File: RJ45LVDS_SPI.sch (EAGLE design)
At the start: 45 parts, among them J1 RJHSE-3381, U1 SN65MLVD206, U2 SN65MLVD206, U3 SN65MLVD206, U4 SN65MLVD206, U5 SN74LVC1T45DBVR, U6 SN74LVC1T45DBVR, U7 SN74LVC1T45DBVR, U8 SN74LVC1T45DBVR, U9 MIC39100-3.3WS

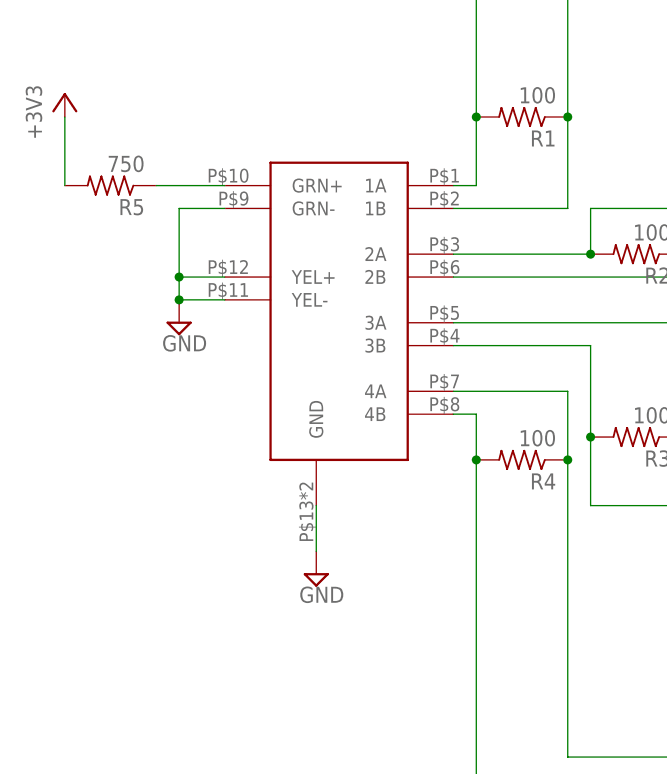
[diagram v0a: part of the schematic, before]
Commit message: Changed RJ45 footprint
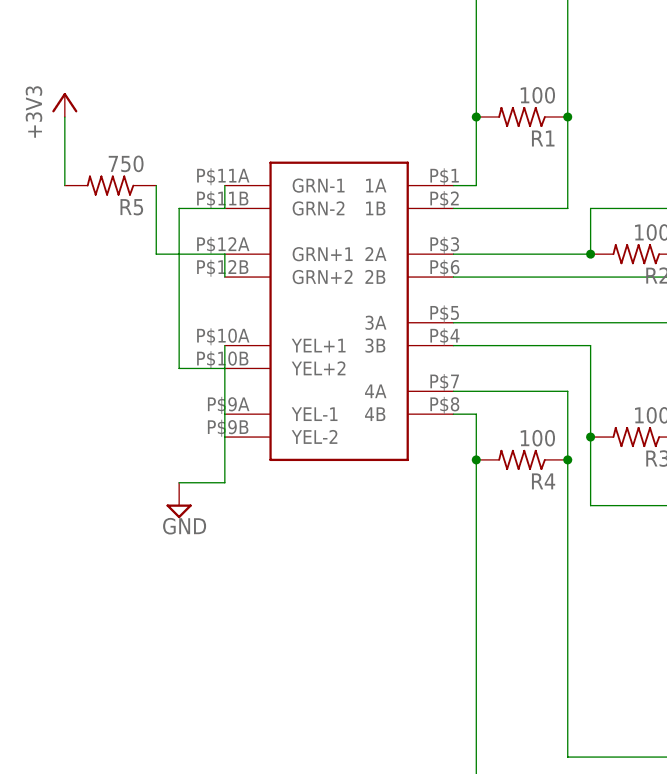
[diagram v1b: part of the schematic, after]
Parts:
- removed J1: RJHSE-3381, artiq-ttl:RJHSE-3381
- added J2: MRJ, artiq-ttl:MRJ
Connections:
- net GND: now also J2.GRN-1, J2.GRN-2, J2.YEL+1, J2.YEL+2, J2.YEL-1, J2.YEL-2; no longer J1.GND, J1.GRN-, J1.YEL+, J1.YEL-
- net IN1_N: now also J2.1B; no longer J1.1B
- net IN1_P: now also J2.1A; no longer J1.1A
- net IN2_N: now also J2.2B; no longer J1.2B
- net IN2_P: now also J2.2A; no longer J1.2A
- net IN3_N: now also J2.3B; no longer J1.3B
- net IN3_P: now also J2.3A; no longer J1.3A
- net IN4_N: now also J2.4B; no longer J1.4B
- net IN4_P: now also J2.4A; no longer J1.4A
- net N$19: now also J2.GRN+1, J2.GRN+2; no longer J1.GRN+

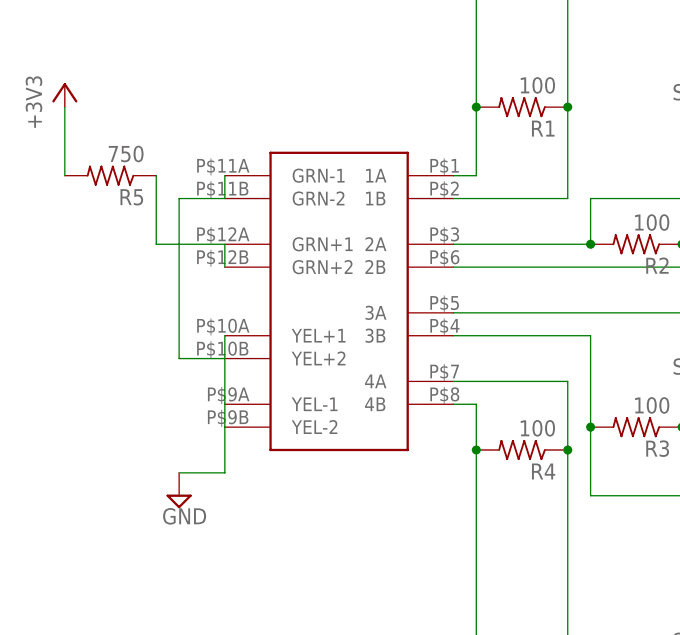
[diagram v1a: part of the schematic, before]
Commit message: Fixed RJ45 footprint issue
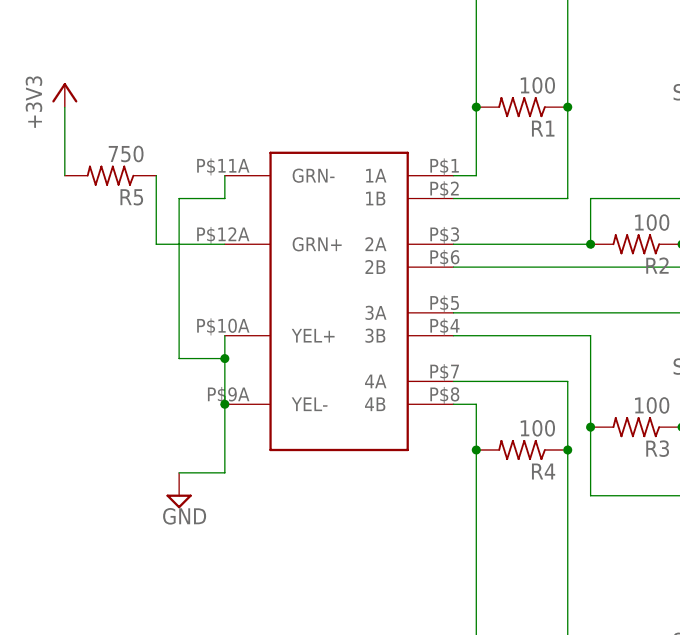
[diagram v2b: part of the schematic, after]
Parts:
- removed J2: MRJ, artiq-ttl:MRJ
- added J1: MRJ, RJ45LVDS_SPI:MRJ
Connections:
- net GND: now also J1.GRN-, J1.YEL+, J1.YEL-; no longer J2.GRN-1, J2.GRN-2, J2.YEL+1, J2.YEL+2, J2.YEL-1, J2.YEL-2
- net IN1_N: now also J1.1B; no longer J2.1B
- net IN1_P: now also J1.1A; no longer J2.1A
- net IN2_N: now also J1.2B; no longer J2.2B
- net IN2_P: now also J1.2A; no longer J2.2A
- net IN3_N: now also J1.3B; no longer J2.3B
- net IN3_P: now also J1.3A; no longer J2.3A
- net IN4_N: now also J1.4B; no longer J2.4B
- net IN4_P: now also J1.4A; no longer J2.4A
- net N$19: now also J1.GRN+; no longer J2.GRN+1, J2.GRN+2
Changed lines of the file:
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@@
 <part name="+3V8" library="supply1" deviceset="+3V3" device=""/>
 <part name="+3V9" library="supply1" deviceset="+3V3" device=""/>
-<part name="J2" library="artiq-ttl" deviceset="MRJ" device=""/>
+<part name="J1" library="RJ45LVDS_SPI" deviceset="MRJ" device=""/>
 </parts>
 <sheets>
@@
 <instance part="+3V8" gate="G$1" x="40.64" y="160.02"/>
 <instance part="+3V9" gate="G$1" x="114.3" y="127"/>
-<instance part="J2" gate="G$1" x="-78.74" y="58.42"/>
+<instance part="J1" gate="G$1" x="-78.74" y="58.42"/>
 </instances>
 <busses>
@@
 <pinref part="R4" gate="G$1" pin="1"/>
 <junction x="-55.88" y="43.18"/>
-<pinref part="J2" gate="G$1" pin="4A"/>
+<pinref part="J1" gate="G$1" pin="4A"/>
 </segment>
 </net>
@@
 <wire x1="-43.18" y1="45.72" x2="-43.18" y2="40.64" width="0.1524" layer="91"/>
 <junction x="-43.18" y="45.72"/>
-<pinref part="J2" gate="G$1" pin="3A"/>
+<pinref part="J1" gate="G$1" pin="3A"/>
 </segment>
 </net>
@@
 <pinref part="R2" gate="G$1" pin="2"/>
 <junction x="-53.34" y="66.04"/>
-<pinref part="J2" gate="G$1" pin="2A"/>
+<pinref part="J1" gate="G$1" pin="2A"/>
 </segment>
 </net>
@@
 <wire x1="-66.04" y1="81.28" x2="-66.04" y2="73.66" width="0.1524" layer="91"/>
 <junction x="-66.04" y="81.28"/>
-<pinref part="J2" gate="G$1" pin="1A"/>
+<pinref part="J1" gate="G$1" pin="1A"/>
 </segment>
 </net>
@@
 <junction x="-55.88" y="81.28"/>
 <wire x1="-68.58" y1="71.12" x2="-55.88" y2="71.12" width="0.1524" layer="91"/>
-<pinref part="J2" gate="G$1" pin="1B"/>
+<pinref part="J1" gate="G$1" pin="1B"/>
 </segment>
 </net>
@@
 <pinref part="R2" gate="G$1" pin="1"/>
 <junction x="-43.18" y="66.04"/>
-<pinref part="J2" gate="G$1" pin="2B"/>
+<pinref part="J1" gate="G$1" pin="2B"/>
 </segment>
 </net>
@@
 <pinref part="R3" gate="G$1" pin="2"/>
 <junction x="-53.34" y="45.72"/>
-<pinref part="J2" gate="G$1" pin="3B"/>
+<pinref part="J1" gate="G$1" pin="3B"/>
 </segment>
 </net>
@@
 <pinref part="R4" gate="G$1" pin="2"/>
 <junction x="-66.04" y="43.18"/>
-<pinref part="J2" gate="G$1" pin="4B"/>
+<pinref part="J1" gate="G$1" pin="4B"/>
 </segment>
 </net>
@@
 </segment>
 <segment>
-<pinref part="J2" gate="G$1" pin="GRN-1"/>
-<pinref part="J2" gate="G$1" pin="GRN-2"/>
+<pinref part="SUPPLY28" gate="GND" pin="GND"/>
+<wire x1="-93.98" y1="40.64" x2="-99.06" y2="40.64" width="0.1524" layer="91"/>
+<wire x1="-93.98" y1="48.26" x2="-93.98" y2="40.64" width="0.1524" layer="91"/>
+<pinref part="J1" gate="G$1" pin="YEL-"/>
+<junction x="-93.98" y="48.26"/>
+<wire x1="-93.98" y1="55.88" x2="-93.98" y2="53.34" width="0.1524" layer="91"/>
+<pinref part="J1" gate="G$1" pin="YEL+"/>
+<wire x1="-93.98" y1="53.34" x2="-93.98" y2="48.26" width="0.1524" layer="91"/>
 <wire x1="-93.98" y1="71.12" x2="-93.98" y2="73.66" width="0.1524" layer="91"/>
 <wire x1="-93.98" y1="71.12" x2="-99.06" y2="71.12" width="0.1524" layer="91"/>
 <wire x1="-99.06" y1="71.12" x2="-99.06" y2="53.34" width="0.1524" layer="91"/>
-<pinref part="J2" gate="G$1" pin="YEL-2"/>
-<pinref part="J2" gate="G$1" pin="YEL-1"/>
-<wire x1="-93.98" y1="45.72" x2="-93.98" y2="48.26" width="0.1524" layer="91"/>
-<pinref part="J2" gate="G$1" pin="YEL+2"/>
-<wire x1="-93.98" y1="48.26" x2="-93.98" y2="53.34" width="0.1524" layer="91"/>
-<pinref part="J2" gate="G$1" pin="YEL+1"/>
-<wire x1="-93.98" y1="53.34" x2="-93.98" y2="55.88" width="0.1524" layer="91"/>
+<pinref part="J1" gate="G$1" pin="GRN-"/>
 <wire x1="-99.06" y1="53.34" x2="-93.98" y2="53.34" width="0.1524" layer="91"/>
-<wire x1="-93.98" y1="45.72" x2="-93.98" y2="40.64" width="0.1524" layer="91"/>
-<pinref part="SUPPLY28" gate="GND" pin="GND"/>
-<wire x1="-93.98" y1="40.64" x2="-99.06" y2="40.64" width="0.1524" layer="91"/>
+<junction x="-93.98" y="53.34"/>
 </segment>
 </net>
@@
 <net name="N$19" class="0">
 <segment>
-<pinref part="J2" gate="G$1" pin="GRN+2"/>
-<pinref part="J2" gate="G$1" pin="GRN+1"/>
-<wire x1="-93.98" y1="63.5" x2="-93.98" y2="66.04" width="0.1524" layer="91"/>
 <wire x1="-93.98" y1="66.04" x2="-101.6" y2="66.04" width="0.1524" layer="91"/>
 <pinref part="R5" gate="G$1" pin="1"/>
 <wire x1="-101.6" y1="66.04" x2="-101.6" y2="73.66" width="0.1524" layer="91"/>
-</segment>
-</net>
+<pinref part="J1" gate="G$1" pin="GRN+"/>
+</segment>
+</net>

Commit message: v0.4 changes
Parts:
- added C17: .1u, rcl-dhs:C-USC0603
- added JP3: (no value), pinhead:PINHD-1X2
- added U10: 74AHC1GU04DCK, 74xx-little-us:74AHC1GU04DCK
- JP1: device pinhead:PINHD-2X5 -> pinhead:PINHD-2X6
- SJ1, SJ2, SJ3, SJ4, SJ5, SJ6, SJ7, SJ8: device jumper:SJ2W -> RJ45LVDS_SPI:SJ2W
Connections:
- new net A: JP3.1, U10G$1.I
- new net NOT_A: JP3.2, U10G$1.O
- net +3V3: now also JP1.1, JP1.2
- net GND: now also C17.2, JP1.3, JP1.4, U10G$2.GND; no longer JP1.1, JP1.2
- net N$13: now also JP1.5, JP1.6; no longer JP1.3, JP1.4
- net N$14: now also JP1.7, JP1.8; no longer JP1.5, JP1.6
- net N$15: now also JP1.10, JP1.9; no longer JP1.7, JP1.8
- net N$8: now also JP1.11, JP1.12; no longer JP1.10, JP1.9
- net VCCIO: now also C17.1, U10G$2.VCC
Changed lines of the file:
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@@
 <layer number="91" name="Nets" color="2" fill="1" visible="yes" active="yes"/>
 <layer number="92" name="Busses" color="1" fill="1" visible="yes" active="yes"/>
-<layer number="93" name="Pins" color="2" fill="1" visible="no" active="yes"/>
+<layer number="93" name="Pins" color="2" fill="1" visible="yes" active="yes"/>
 <layer number="94" name="Symbols" color="4" fill="1" visible="yes" active="yes"/>
 <layer number="95" name="Names" color="7" fill="1" visible="yes" active="yes"/>
@@
 <part name="C8" library="rcl-dhs" deviceset="C-US" device="C0603" value=".1u"/>
 <part name="SUPPLY28" library="supply2" deviceset="GND" device=""/>
-<part name="SJ1" library="jumper" deviceset="SJ2W" device=""/>
-<part name="SJ2" library="jumper" deviceset="SJ2W" device=""/>
-<part name="SJ3" library="jumper" deviceset="SJ2W" device=""/>
-<part name="SJ4" library="jumper" deviceset="SJ2W" device=""/>
+<part name="SJ1" library="RJ45LVDS_SPI" deviceset="SJ2W" device=""/>
+<part name="SJ2" library="RJ45LVDS_SPI" deviceset="SJ2W" device=""/>
+<part name="SJ3" library="RJ45LVDS_SPI" deviceset="SJ2W" device=""/>
+<part name="SJ4" library="RJ45LVDS_SPI" deviceset="SJ2W" device=""/>
 <part name="U5" library="SN74LVC1T45DBVR" deviceset="SN74LVC1T45DBVR" device=""/>
 <part name="U6" library="SN74LVC1T45DBVR" deviceset="SN74LVC1T45DBVR" device=""/>
@@
 <part name="U8" library="SN74LVC1T45DBVR" deviceset="SN74LVC1T45DBVR" device=""/>
 <part name="+3V6" library="supply1" deviceset="+3V3" device=""/>
-<part name="SJ5" library="jumper" deviceset="SJ2W" device=""/>
-<part name="SJ6" library="jumper" deviceset="SJ2W" device=""/>
-<part name="SJ7" library="jumper" deviceset="SJ2W" device=""/>
-<part name="SJ8" library="jumper" deviceset="SJ2W" device=""/>
+<part name="SJ5" library="RJ45LVDS_SPI" deviceset="SJ2W" device=""/>
+<part name="SJ6" library="RJ45LVDS_SPI" deviceset="SJ2W" device=""/>
+<part name="SJ7" library="RJ45LVDS_SPI" deviceset="SJ2W" device=""/>
+<part name="SJ8" library="RJ45LVDS_SPI" deviceset="SJ2W" device=""/>
 <part name="SUPPLY6" library="supply2" deviceset="GND" device=""/>
 <part name="SJ9" library="rcl-dhs" deviceset="JUMPER" device=""/>
@@
 <part name="C6" library="rcl-dhs" deviceset="C-US" device="C0603" value=".1u"/>
 <part name="C7" library="rcl-dhs" deviceset="C-US" device="C0603" value=".1u"/>
-<part name="JP1" library="pinhead" deviceset="PINHD-2X5" device=""/>
 <part name="JP2" library="pinhead" deviceset="PINHD-1X4" device=""/>
 <part name="C12" library="rcl-dhs" deviceset="C-US" device="C0603" value=".1u"/>
@@
 <part name="+3V9" library="supply1" deviceset="+3V3" device=""/>
 <part name="J1" library="RJ45LVDS_SPI" deviceset="MRJ" device=""/>
+<part name="JP1" library="pinhead" deviceset="PINHD-2X6" device=""/>
+<part name="+3V10" library="supply1" deviceset="+3V3" device=""/>
+<part name="U10" library="74xx-little-us" deviceset="74*1GU04" device="DCK" technology="AHC"/>
+<part name="JP3" library="pinhead" deviceset="PINHD-1X2" device=""/>
+<part name="VCC4" library="supply1" deviceset="VCCIO" device=""/>
+<part name="SUPPLY1" library="supply2" deviceset="GND" device=""/>
+<part name="C17" library="rcl-dhs" deviceset="C-US" device="C0603" value=".1u"/>
 </parts>
 <sheets>
@@
 <instance part="C6" gate="G$1" x="55.88" y="187.96"/>
 <instance part="C7" gate="G$1" x="66.04" y="187.96"/>
-<instance part="JP1" gate="A" x="160.02" y="53.34"/>
 <instance part="JP2" gate="A" x="180.34" y="106.68"/>
 <instance part="C12" gate="G$1" x="111.76" y="157.48" rot="R180"/>
@@
 <instance part="+3V9" gate="G$1" x="114.3" y="127"/>
 <instance part="J1" gate="G$1" x="-78.74" y="58.42"/>
+<instance part="JP1" gate="A" x="160.02" y="55.88"/>
+<instance part="+3V10" gate="G$1" x="149.86" y="71.12"/>
+<instance part="U10" gate="G$1" x="-91.44" y="147.32"/>
+<instance part="JP3" gate="G$1" x="-88.9" y="127" rot="R90"/>
+<instance part="U10" gate="G$2" x="-68.58" y="180.34"/>
+<instance part="VCC4" gate="G$1" x="-68.58" y="198.12"/>
+<instance part="SUPPLY1" gate="GND" x="-68.58" y="165.1"/>
+<instance part="C17" gate="G$1" x="165.1" y="157.48"/>
 </instances>
 <busses>
@@
 <segment>
 <pinref part="SUPPLY34" gate="GND" pin="GND"/>
-<pinref part="JP1" gate="A" pin="1"/>
-<pinref part="JP1" gate="A" pin="2"/>
 <wire x1="175.26" y1="58.42" x2="175.26" y2="53.34" width="0.1524" layer="91"/>
+<wire x1="165.1" y1="58.42" x2="175.26" y2="58.42" width="0.1524" layer="91"/>
+<pinref part="JP1" gate="A" pin="4"/>
+<pinref part="JP1" gate="A" pin="3"/>
 <wire x1="157.48" y1="58.42" x2="165.1" y2="58.42" width="0.1524" layer="91"/>
-<wire x1="165.1" y1="58.42" x2="175.26" y2="58.42" width="0.1524" layer="91"/>
 <junction x="165.1" y="58.42"/>
 </segment>
@@
 <wire x1="152.4" y1="154.94" x2="152.4" y2="152.4" width="0.1524" layer="91"/>
 <junction x="152.4" y="152.4"/>
+<pinref part="C17" gate="G$1" pin="2"/>
+<wire x1="165.1" y1="152.4" x2="157.48" y2="152.4" width="0.1524" layer="91"/>
+<junction x="157.48" y="152.4"/>
 </segment>
 <segment>
@@
 <wire x1="-99.06" y1="53.34" x2="-93.98" y2="53.34" width="0.1524" layer="91"/>
 <junction x="-93.98" y="53.34"/>
+</segment>
+<segment>
+<pinref part="U10" gate="G$2" pin="GND"/>
+<pinref part="SUPPLY1" gate="GND" pin="GND"/>
+<wire x1="-68.58" y1="172.72" x2="-68.58" y2="167.64" width="0.1524" layer="91"/>
 </segment>
 </net>
@@
 <pinref part="+3V9" gate="G$1" pin="+3V3"/>
 </segment>
+<segment>
+<pinref part="+3V10" gate="G$1" pin="+3V3"/>
+<wire x1="149.86" y1="68.58" x2="149.86" y2="60.96" width="0.1524" layer="91"/>
+<pinref part="JP1" gate="A" pin="1"/>
+<wire x1="149.86" y1="60.96" x2="157.48" y2="60.96" width="0.1524" layer="91"/>
+<pinref part="JP1" gate="A" pin="2"/>
+<wire x1="157.48" y1="60.96" x2="165.1" y2="60.96" width="0.1524" layer="91"/>
+<junction x="157.48" y="60.96"/>
+</segment>
 </net>
 <net name="3_33" class="0">
@@
 <pinref part="U5" gate="A" pin="B"/>
 <wire x1="104.14" y1="91.44" x2="104.14" y2="99.06" width="0.1524" layer="91"/>
-<pinref part="JP1" gate="A" pin="3"/>
 <wire x1="157.48" y1="55.88" x2="144.78" y2="55.88" width="0.1524" layer="91"/>
 <wire x1="144.78" y1="55.88" x2="144.78" y2="58.42" width="0.1524" layer="91"/>
 <wire x1="144.78" y1="58.42" x2="137.16" y2="58.42" width="0.1524" layer="91"/>
-<pinref part="JP1" gate="A" pin="4"/>
-<wire x1="157.48" y1="55.88" x2="165.1" y2="55.88" width="0.1524" layer="91"/>
+<pinref part="JP1" gate="A" pin="5"/>
+<pinref part="JP1" gate="A" pin="6"/>
+<wire x1="165.1" y1="55.88" x2="157.48" y2="55.88" width="0.1524" layer="91"/>
 <junction x="157.48" y="55.88"/>
 </segment>
@@
 <wire x1="132.08" y1="55.88" x2="142.24" y2="55.88" width="0.1524" layer="91"/>
 <wire x1="142.24" y1="55.88" x2="142.24" y2="53.34" width="0.1524" layer="91"/>
-<pinref part="JP1" gate="A" pin="5"/>
 <wire x1="157.48" y1="53.34" x2="142.24" y2="53.34" width="0.1524" layer="91"/>
-<pinref part="JP1" gate="A" pin="6"/>
+<pinref part="JP1" gate="A" pin="7"/>
+<pinref part="JP1" gate="A" pin="8"/>
 <wire x1="157.48" y1="53.34" x2="165.1" y2="53.34" width="0.1524" layer="91"/>
 <junction x="157.48" y="53.34"/>
@@
 <wire x1="132.08" y1="38.1" x2="104.14" y2="38.1" width="0.1524" layer="91"/>
 <wire x1="104.14" y1="38.1" x2="104.14" y2="45.72" width="0.1524" layer="91"/>
-<pinref part="JP1" gate="A" pin="7"/>
 <wire x1="157.48" y1="50.8" x2="139.7" y2="50.8" width="0.1524" layer="91"/>
 <wire x1="139.7" y1="50.8" x2="139.7" y2="53.34" width="0.1524" layer="91"/>
 <wire x1="139.7" y1="53.34" x2="132.08" y2="53.34" width="0.1524" layer="91"/>
-<pinref part="JP1" gate="A" pin="8"/>
+<pinref part="JP1" gate="A" pin="9"/>
+<pinref part="JP1" gate="A" pin="10"/>
 <wire x1="157.48" y1="50.8" x2="165.1" y2="50.8" width="0.1524" layer="91"/>
 <junction x="157.48" y="50.8"/>
@@
 <wire x1="104.14" y1="12.7" x2="137.16" y2="12.7" width="0.1524" layer="91"/>
 <wire x1="137.16" y1="12.7" x2="137.16" y2="48.26" width="0.1524" layer="91"/>
-<pinref part="JP1" gate="A" pin="9"/>
 <wire x1="157.48" y1="48.26" x2="137.16" y2="48.26" width="0.1524" layer="91"/>
-<pinref part="JP1" gate="A" pin="10"/>
+<pinref part="JP1" gate="A" pin="11"/>
+<pinref part="JP1" gate="A" pin="12"/>
 <wire x1="157.48" y1="48.26" x2="165.1" y2="48.26" width="0.1524" layer="91"/>
 <junction x="157.48" y="48.26"/>
@@
 <wire x1="104.14" y1="162.56" x2="104.14" y2="167.64" width="0.1524" layer="91"/>
 <junction x="111.76" y="162.56"/>
+<pinref part="C17" gate="G$1" pin="1"/>
+<wire x1="165.1" y1="160.02" x2="165.1" y2="162.56" width="0.1524" layer="91"/>
+<wire x1="165.1" y1="162.56" x2="152.4" y2="162.56" width="0.1524" layer="91"/>
+<junction x="152.4" y="162.56"/>
 </segment>
 <segment>
@@
 <junction x="137.16" y="119.38"/>
 </segment>
+<segment>
+<pinref part="VCC4" gate="G$1" pin="VCCIO"/>
+<pinref part="U10" gate="G$2" pin="VCC"/>
+<wire x1="-68.58" y1="195.58" x2="-68.58" y2="187.96" width="0.1524" layer="91"/>
+</segment>
 </net>
 <net name="N$19" class="0">
@@
 </segment>
 </net>
+<net name="A" class="0">
+<segment>
+<pinref part="U10" gate="G$1" pin="I"/>
+<wire x1="-101.6" y1="147.32" x2="-104.14" y2="147.32" width="0.1524" layer="91"/>
+<wire x1="-104.14" y1="147.32" x2="-104.14" y2="134.62" width="0.1524" layer="91"/>
+<pinref part="JP3" gate="G$1" pin="1"/>
+<wire x1="-104.14" y1="134.62" x2="-91.44" y2="134.62" width="0.1524" layer="91"/>
+<wire x1="-91.44" y1="134.62" x2="-91.44" y2="124.46" width="0.1524" layer="91"/>
+</segment>
+</net>
+<net name="NOT_A" class="0">
+<segment>
+<pinref part="JP3" gate="G$1" pin="2"/>
+<wire x1="-88.9" y1="124.46" x2="-88.9" y2="134.62" width="0.1524" layer="91"/>
+<wire x1="-88.9" y1="134.62" x2="-63.5" y2="134.62" width="0.1524" layer="91"/>
+<wire x1="-63.5" y1="134.62" x2="-63.5" y2="147.32" width="0.1524" layer="91"/>
+<pinref part="U10" gate="G$1" pin="O"/>
+<wire x1="-63.5" y1="147.32" x2="-81.28" y2="147.32" width="0.1524" layer="91"/>
+</segment>
+</net>
